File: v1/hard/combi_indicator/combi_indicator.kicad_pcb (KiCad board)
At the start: 2 copper layers, 71 x 44 mm, 36 parts, among them J1 Conn_01x04_Male, U1 HT7991

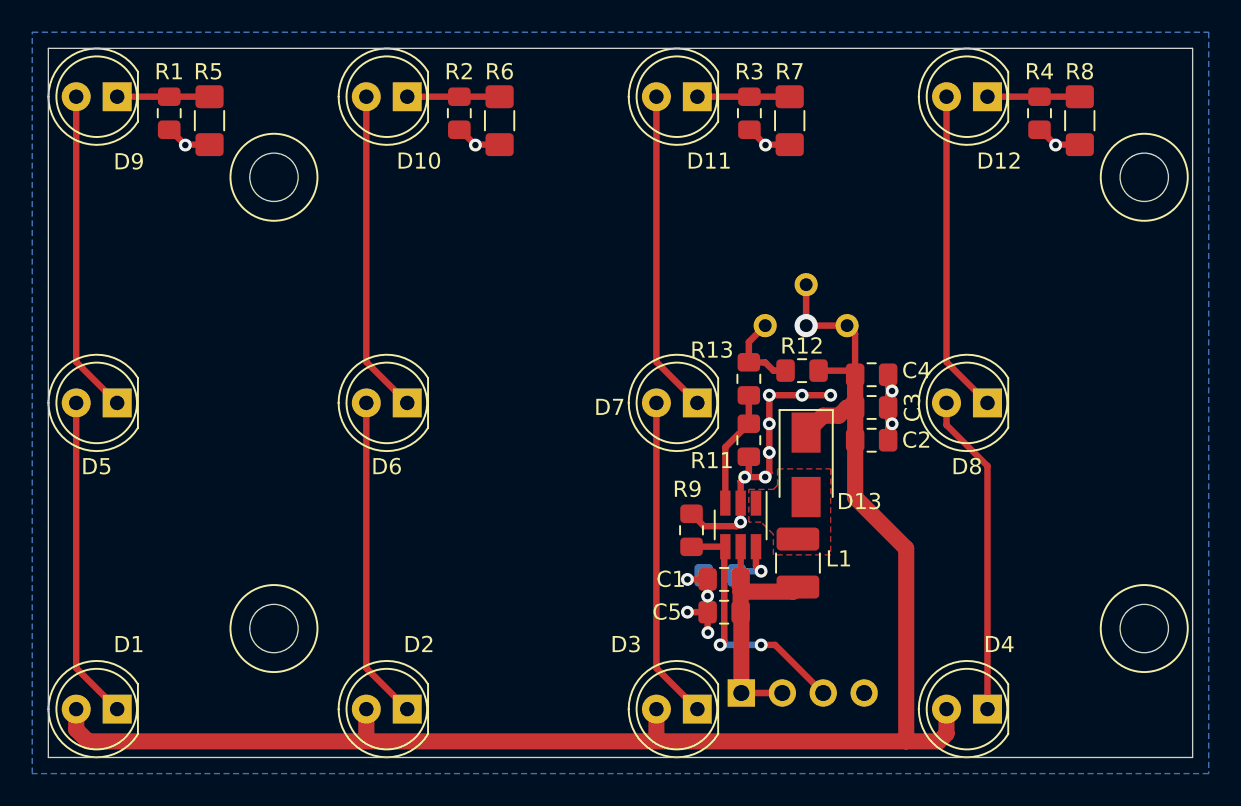
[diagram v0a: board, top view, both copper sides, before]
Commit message: Moved connectors location to 2.54 grid for better compartibility with predrilled prototyping boards.
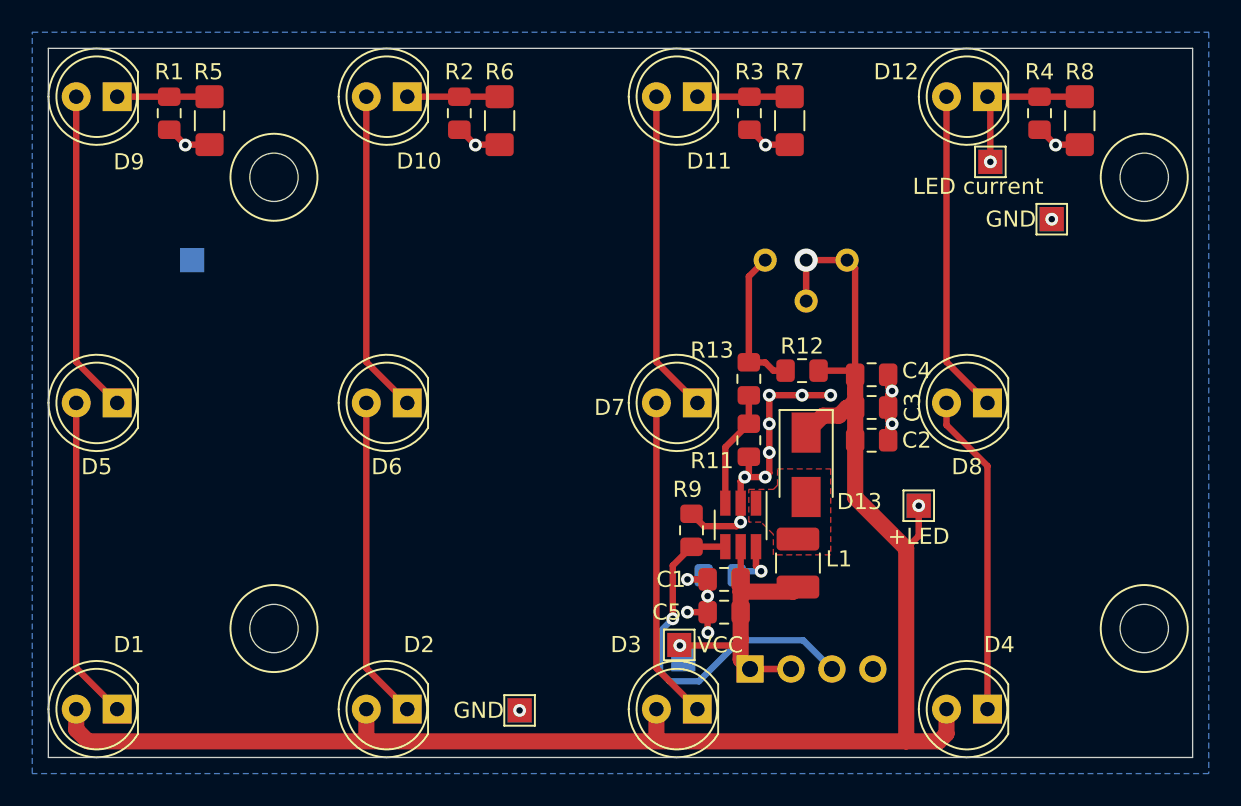
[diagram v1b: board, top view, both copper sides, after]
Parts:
- added +LED: TestPoint_Pad_1.5x1.5mm, TestPoint:TestPoint_Pad_1.5x1.5mm, B.Cu at (113.0, 106.4)
- added +LED: TestPoint_Pad_1.5x1.5mm, TestPoint:TestPoint_Pad_1.5x1.5mm, F.Cu at (113.0, 106.4)
- added GND: TestPoint_Pad_1.5x1.5mm, TestPoint:TestPoint_Pad_1.5x1.5mm, F.Cu at (121.3, 88.6)
- added GND: TestPoint_Pad_1.5x1.5mm, TestPoint:TestPoint_Pad_1.5x1.5mm, F.Cu at (88.2, 119.1)
- added GND: TestPoint_Pad_1.5x1.5mm, TestPoint:TestPoint_Pad_1.5x1.5mm, B.Cu at (88.2, 119.1)
- added GND: TestPoint_Pad_1.5x1.5mm, TestPoint:TestPoint_Pad_1.5x1.5mm, B.Cu at (67.9, 91.1)
- added GND: TestPoint_Pad_1.5x1.5mm, TestPoint:TestPoint_Pad_1.5x1.5mm, B.Cu at (121.3, 88.6)
- added LED current: TestPoint_Pad_1.5x1.5mm, TestPoint:TestPoint_Pad_1.5x1.5mm, F.Cu at (117.5, 85.0)
- added LED current: TestPoint_Pad_1.5x1.5mm, TestPoint:TestPoint_Pad_1.5x1.5mm, B.Cu at (117.5, 85.0)
- added VCC: TestPoint_Pad_1.5x1.5mm, TestPoint:TestPoint_Pad_1.5x1.5mm, F.Cu at (98.1, 115.0)
- added VCC: TestPoint_Pad_1.5x1.5mm, TestPoint:TestPoint_Pad_1.5x1.5mm, B.Cu at (98.4, 115.9)
- moved RV1 6.51 mm to (108.6, 91.1), turned to 270 degrees
- moved J1 1.58 mm to (102.5, 116.5)
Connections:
- net Net-(D12-Pad1) renamed /cur_test
- RV1 pad 1: Net-(R12-Pad2) -> VBUS
- RV1 pad 3: VBUS -> Net-(R12-Pad2)
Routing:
- net /OPT_E: track 16.0 -> 23.4 mm, vias 2 -> 1
- net VBUS: track 99.2 -> 106.2 mm, vias 1 -> 2
- net /cur_test: track 5.73 -> 9.85 mm, vias 0 -> 1
- net Net-(R12-Pad2): track 5.19 -> 9.25 mm
- net VCC: track 15.4 -> 19.0 mm, vias 0 -> 1
- net GND: vias 18 -> 20

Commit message: Finished "combi indicator" - indicator board for combi button, v0.1. Added table with resistor values for LED of different color. Also provided spreadsheet with all formulas.
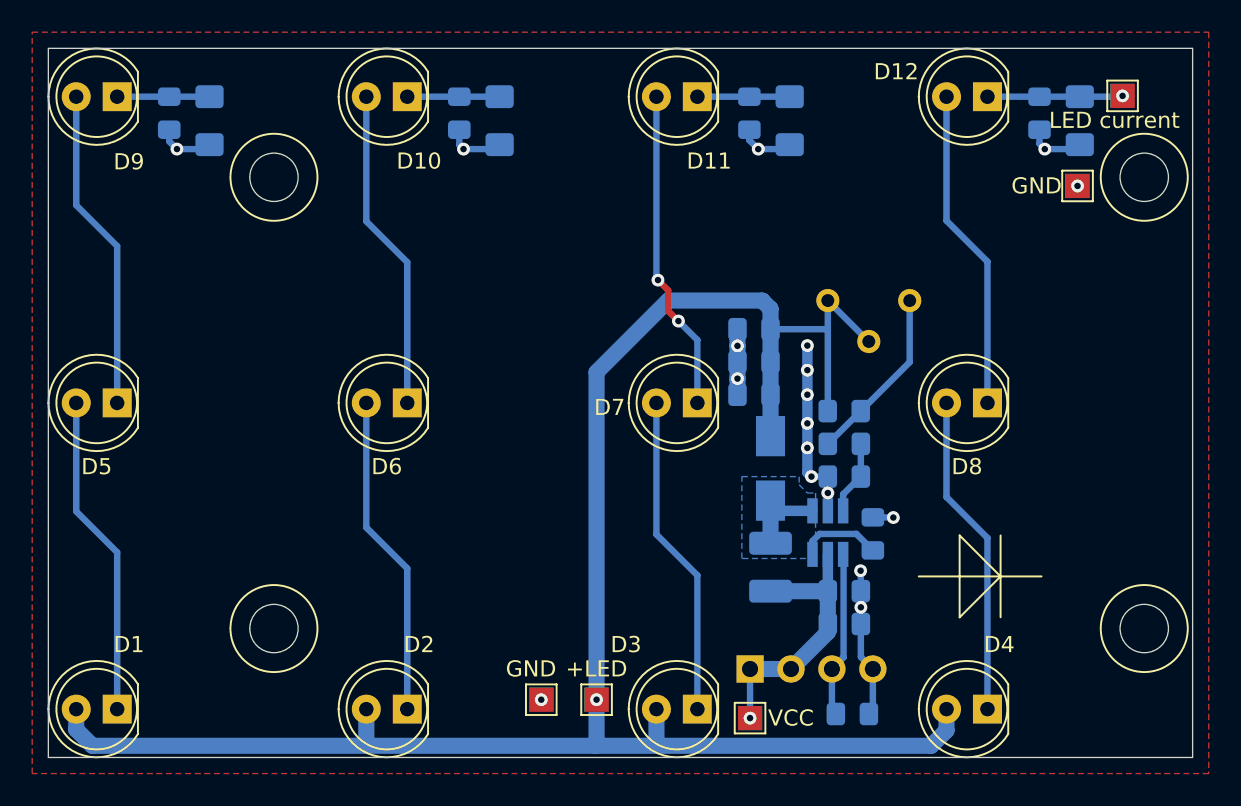
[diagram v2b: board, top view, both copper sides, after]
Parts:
- removed the GND at (88.2, 119.1)
- removed the GND at (67.9, 91.1)
- added GND: TestPoint_Pad_1.5x1.5mm, TestPoint:TestPoint_Pad_1.5x1.5mm, B.Cu at (89.6, 118.4)
- C1, C2, C3, C4, C5, D13, L1, R1, R11, R2, R3, R4, R5, R6, R7, R8, R9, U1: moved to B.Cu
- R12: value 232k 1% -> 200k; moved to B.Cu
- R13: value 82.5k 1% -> 82k; moved to B.Cu
- moved +LED 23.3 mm to (93.0, 118.4) (x2)
- moved REF** 21.7 mm to (71.0, 105.0)
- moved R9 15.2 mm to (108.9, 119.3), turned to 0 degrees
- moved R10 9.82 mm to (110.2, 108.1), turned to 90 degrees
- moved LED current 9.17 mm to (125.7, 81.0) (x2)
- moved C2 8.77 mm to (102.8, 97.5), turned to 180 degrees
- moved C4 7.83 mm to (102.8, 95.4), turned to 0 degrees
- moved C1 7.50 mm to (108.4, 111.7), turned to 180 degrees
- moved C5 7.50 mm to (108.4, 113.7), turned to 0 degrees
- moved C3 7.34 mm to (102.8, 99.5), turned to 180 degrees
- moved R13 7.17 mm to (108.4, 102.5), turned to 0 degrees
- moved R11 6.34 mm to (108.4, 104.6), turned to 180 degrees
- moved VCC 6.32 mm to (102.5, 119.6)
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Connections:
- RV1 pad 1: VBUS -> Net-(R12-Pad2)
- RV1 pad 3: Net-(R12-Pad2) -> VBUS
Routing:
- net VBUS: track 106.2 -> 119.9 mm, vias 2 -> 1
- net /OPT_E: track 23.4 -> 10.3 mm, vias 1 -> 0
- net /L: track 0.00 -> 5.51 mm
- net /FB: track 7.29 -> 4.61 mm
- net Net-(R10-Pad1): track 3.28 -> 5.18 mm, vias 1 -> 0
- net VCC: track 19.0 -> 17.2 mm
- net Net-(R12-Pad2): track 9.25 -> 11.0 mm
- net /cur_test: track 9.85 -> 8.40 mm
- net GND: track 40.1 -> 40.4 mm, vias 20 -> 18
- net Net-(D11-Pad2): vias 0 -> 2
- added copper zone on B.Cu, net /L
- added copper zone on F.Cu, net GND
- removed copper zone on F.Cu, net /L
- removed copper zone on B.Cu, net GND
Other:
- board text added: "10k"
- board text added: "130u"
- board text added: "140k"
- board text added: "150k"
- board text added: "180u"
- board text added: "270u"
- board text added: "330k"
- board text added: "7k5"
- board text added: "82k"
- board text added: "8k1"
- board text added: "91k"
- board text added: "All values are for 5mA per LED line 20mA in total"
- board text added: "B"
- board text added: "Clr"
- board text added: "G"
- board text added: "L1"
- board text added: "R"
- board text added: "R12"
- board text added: "R13"
- board text added: "Uni"
- board text added: "Y"
